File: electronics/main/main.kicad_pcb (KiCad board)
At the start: 2 copper layers, 113 parts, among them IC1 ATMEGA8-P, J1 CABLE, J2 CABLE, J3 CABLE, J4 CABLE, J5 CABLE, J6 CABLE, J7 CABLE, J8 CABLE, P1 5v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

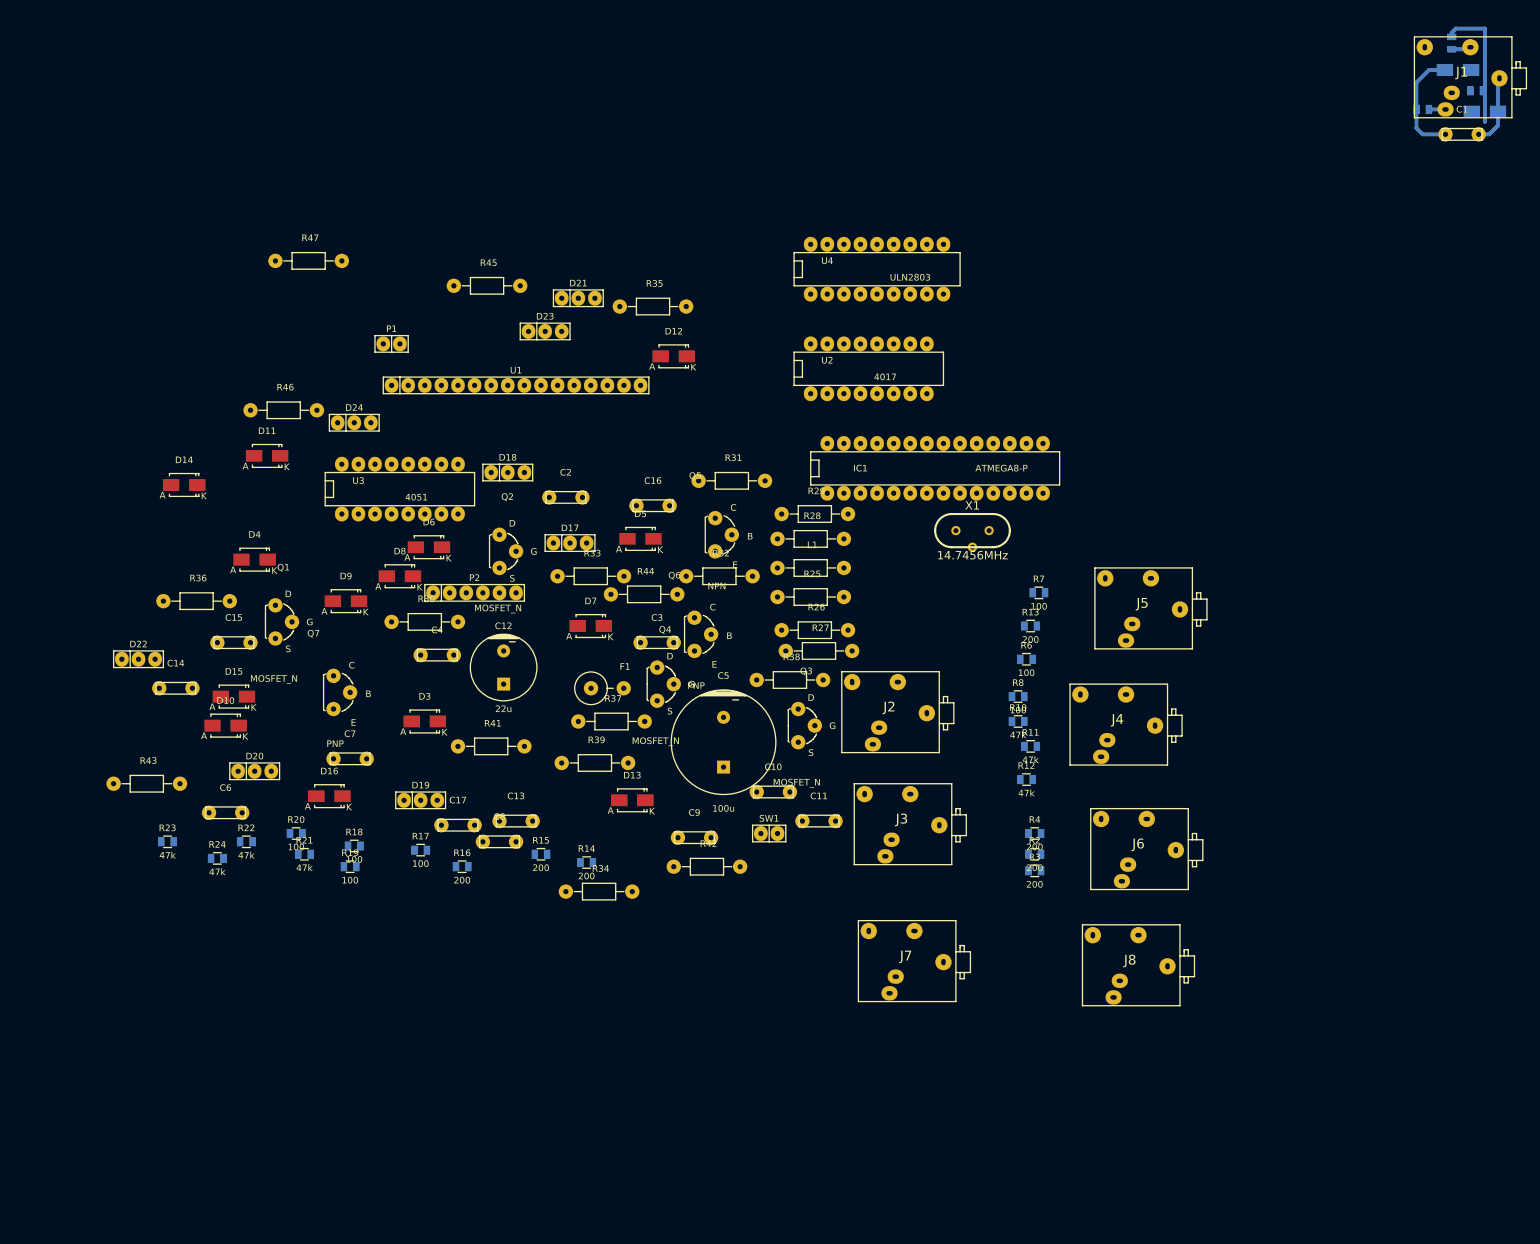
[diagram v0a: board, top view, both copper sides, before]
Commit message: draw inputs on pcb
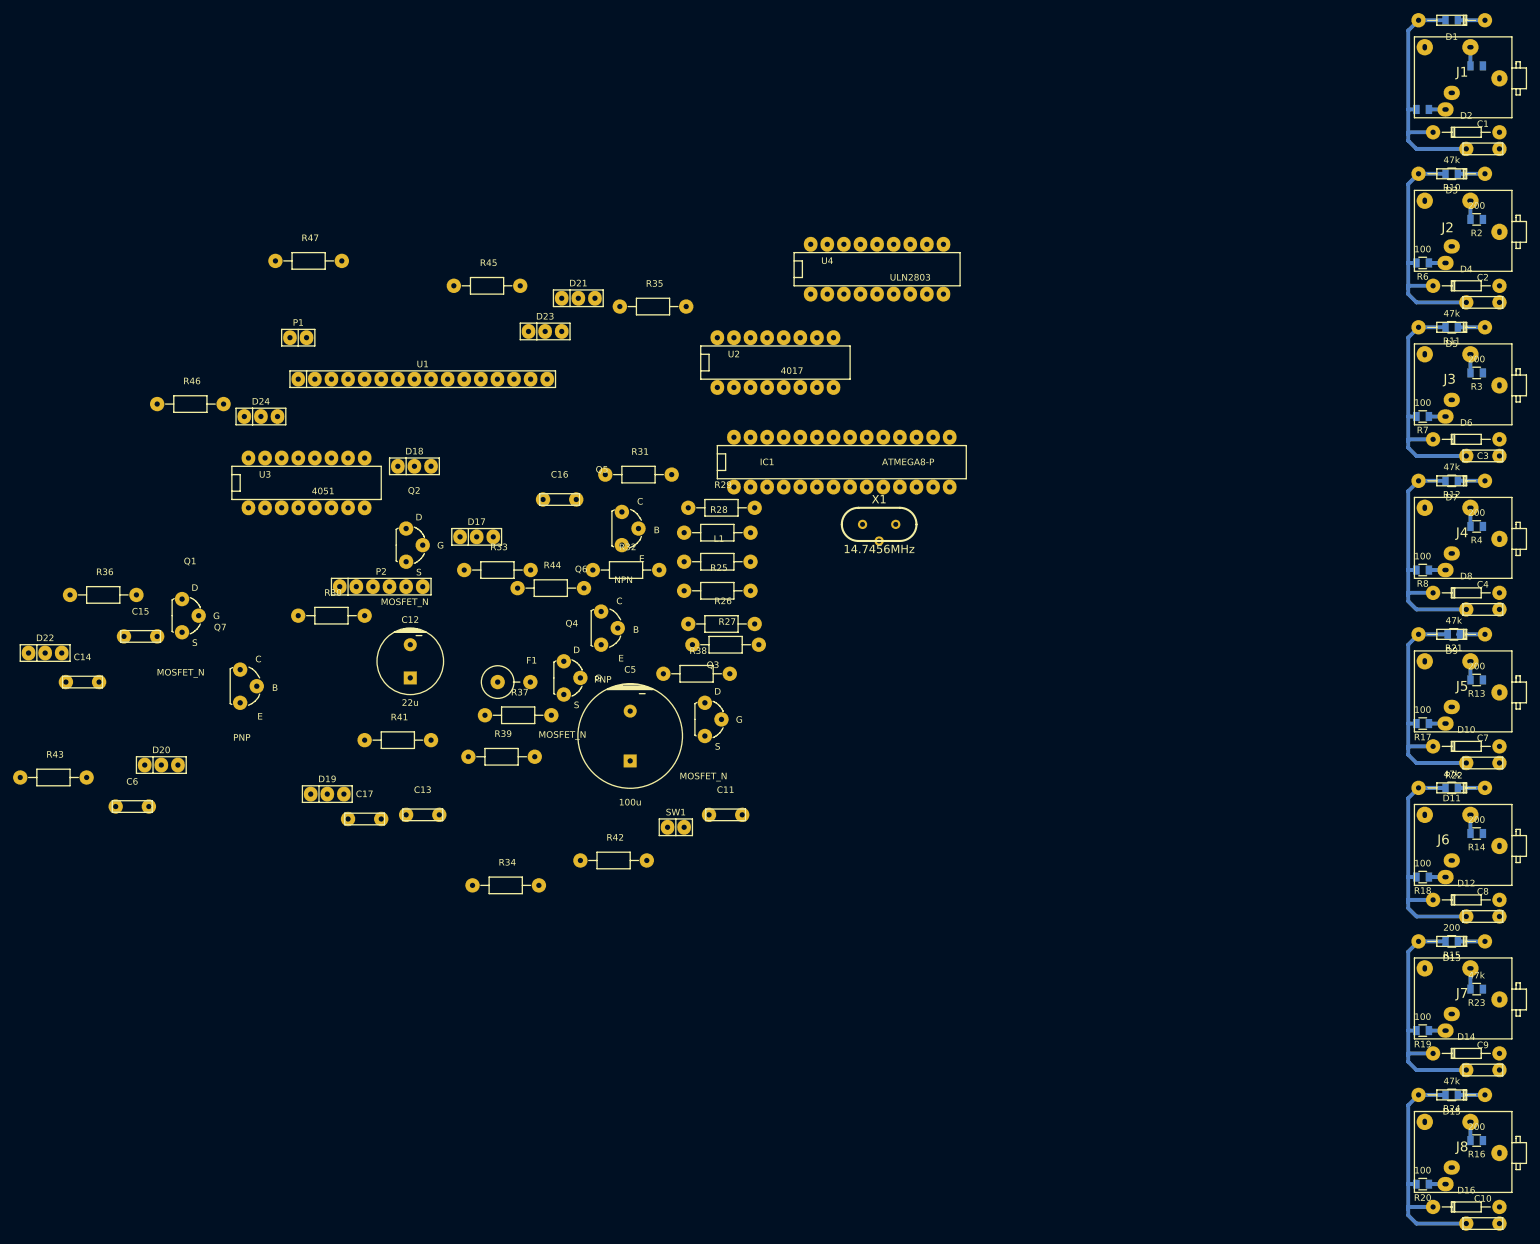
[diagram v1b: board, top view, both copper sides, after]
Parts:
- D1, D2: footprint Diodes_SMD:Diode-SMA_Standard -> Diodes_ThroughHole:Diode_DO-35_SOD27_Horizontal_RM10; moved to F.Cu
- D10, D11, D12, D13, D14, D15, D16, D3, D4, D5, D6, D7, D8, D9: footprint Diodes_SMD:Diode-SMA_Standard -> Diodes_ThroughHole:Diode_DO-35_SOD27_Horizontal_RM10
- moved D14 214.6 mm to (274.3, 175.3), turned to 180 degrees
- moved R23 201.6 mm to (275.9, 165.4), turned to 180 degrees
- moved D15 196.1 mm to (272.1, 181.6)
- moved R24 192.3 mm to (272.1, 181.6), turned to 180 degrees
- moved D4 190.1 mm to (274.3, 57.8), turned to 180 degrees
- moved D10 189.9 mm to (274.3, 128.3), turned to 180 degrees
- moved D11 188.3 mm to (272.1, 134.6)
- moved D16 185.0 mm to (274.3, 198.8), turned to 180 degrees
- moved R22 184.7 mm to (272.1, 134.6), turned to 180 degrees
- moved R20 180.6 mm to (267.7, 195.3), turned to 180 degrees
- moved R21 179.1 mm to (272.4, 111.1), turned to 180 degrees
- moved D3 178.1 mm to (272.1, 40.6)
- moved C7 173.4 mm to (276.9, 130.8)
- moved D9 169.3 mm to (272.1, 111.1)
- moved R19 166.1 mm to (267.7, 171.8), turned to 180 degrees
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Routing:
- net /IN6: track 0.00 -> 38.0 mm
- net /IN7: track 0.00 -> 38.0 mm
- net /IN2: track 0.00 -> 38.0 mm
- net /IN5: track 0.00 -> 38.0 mm
- net /IN4: track 0.00 -> 38.0 mm
- net /IN8: track 0.00 -> 38.0 mm
- net /IN3: track 0.00 -> 38.0 mm
- net /IN1: track 17.0 -> 38.0 mm
- net VCC: track 21.7 -> 33.0 mm
- net GND: track 10.8 -> 0.00 mm
- net Net-(J5-Pad3): track 0.00 -> 2.86 mm
- net Net-(J3-Pad3): track 0.00 -> 2.86 mm
- net Net-(J2-Pad3): track 0.00 -> 2.86 mm
- net Net-(J4-Pad3): track 0.00 -> 2.86 mm
- net Net-(J8-Pad3): track 0.00 -> 2.86 mm
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
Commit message: draw led control
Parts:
- D17, D18, D19, D20, D21, D22, D23, D24: value BI_LED -> BI_LED2
- Q5, Q6, Q7: footprint Housings_TO-92:TO-92-Bipolar-molded-wide-CBE -> Housings_TO-92:TO-92-Free-molded-wide
- moved D1 225.1 mm to (47.1, 24.6), turned to 90 degrees
- moved R9 225.1 mm to (47.1, 24.6), turned to 270 degrees
- moved R1 221.8 mm to (54.1, 20.8), turned to 270 degrees
- moved J1 217.7 mm to (56.0, 23.0), turned to 90 degrees
- moved C1 210.7 mm to (66.8, 19.8), turned to 90 degrees
- moved D2 210.4 mm to (64.3, 22.4), turned to 270 degrees
- moved R5 206.9 mm to (60.8, 29.1), turned to 270 degrees
- moved D3 202.1 mm to (70.6, 24.6), turned to 90 degrees
- moved R10 202.1 mm to (70.6, 24.6), turned to 270 degrees
- moved R2 200.1 mm to (77.6, 20.8), turned to 270 degrees
- moved J2 196.0 mm to (79.5, 23.0), turned to 90 degrees
- moved C2 190.9 mm to (90.3, 19.8), turned to 90 degrees
- moved D4 189.9 mm to (87.8, 22.4), turned to 270 degrees
- moved C10 187.1 mm to (231.3, 19.8), turned to 90 degrees
- moved R6 185.1 mm to (84.3, 29.1), turned to 270 degrees
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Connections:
- D18 pad 1: Net-(D17-Pad1) -> Net-(D18-Pad1)
- D18 pad 2: Net-(D18-Pad2) -> Net-(D17-Pad2)
- D19 pad 1: Net-(D17-Pad1) -> Net-(D19-Pad1)
- D19 pad 2: Net-(D19-Pad2) -> Net-(D17-Pad2)
- D20 pad 1: Net-(D17-Pad1) -> Net-(D20-Pad1)
- D20 pad 2: Net-(D20-Pad2) -> Net-(D17-Pad2)
- D21 pad 1: Net-(D17-Pad1) -> Net-(D21-Pad1)
- D21 pad 2: Net-(D21-Pad2) -> Net-(D17-Pad2)
- D22 pad 1: Net-(D17-Pad1) -> Net-(D22-Pad1)
- D22 pad 2: Net-(D22-Pad2) -> Net-(D17-Pad2)
- D23 pad 1: Net-(D17-Pad1) -> Net-(D23-Pad1)
- D23 pad 2: Net-(D23-Pad2) -> Net-(D17-Pad2)
- D24 pad 1: Net-(D17-Pad1) -> Net-(D24-Pad1)
- D24 pad 2: Net-(D24-Pad2) -> Net-(D17-Pad2)
- R45 pad 2: (no net) -> Net-(Q6-Pad3)
- R47 pad 1: Net-(D17-Pad1) -> Net-(D17-Pad2)
- R47 pad 2: (no net) -> Net-(Q7-Pad3)
- U1 pad 16: (no net) -> Net-(Q5-Pad3)
- U3 pad 1: /IN5 -> /IN4
- U3 pad 12: /IN4 -> /IN8
- U3 pad 13: /IN1 -> /IN7
- U3 pad 14: /IN2 -> /IN6
- U3 pad 15: /IN3 -> /IN5
- U3 pad 2: /IN7 -> /IN3
- U3 pad 4: /IN8 -> /IN2
- U3 pad 5: /IN6 -> /IN1
- U4 pad 1: /L1 -> /L8
- U4 pad 11: Net-(D24-Pad2) -> Net-(D24-Pad1)
- U4 pad 12: Net-(D23-Pad2) -> Net-(D23-Pad1)
- U4 pad 13: Net-(D22-Pad2) -> Net-(D22-Pad1)
- U4 pad 14: Net-(D21-Pad2) -> Net-(D21-Pad1)
- U4 pad 15: Net-(D20-Pad2) -> Net-(D20-Pad1)
- U4 pad 16: Net-(D19-Pad2) -> Net-(D19-Pad1)
- U4 pad 17: Net-(D18-Pad2) -> Net-(D18-Pad1)
- U4 pad 18: Net-(D17-Pad2) -> Net-(D17-Pad1)
- U4 pad 2: /L2 -> /L7
- U4 pad 3: /L3 -> /L6
- U4 pad 4: /L4 -> /L5
- U4 pad 5: /L5 -> /L4
- U4 pad 6: /L6 -> /L3
- U4 pad 7: /L7 -> /L2
- U4 pad 8: /L8 -> /L1
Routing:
- net /IN8: track 38.0 -> 132.0 mm
- net /IN1: track 38.0 -> 117.9 mm
- net /IN7: track 38.0 -> 103.3 mm
- net /IN2: track 38.0 -> 93.7 mm
- net /IN6: track 38.0 -> 82.9 mm
- net GND: track 0.00 -> 33.4 mm
- net /IN3: track 38.0 -> 65.8 mm
- net /IN5: track 38.0 -> 57.9 mm
- net Net-(Q7-Pad2): track 0.00 -> 16.7 mm
- net /L8: track 0.00 -> 15.6 mm
- net /IN4: track 38.0 -> 42.8 mm
- net Net-(D20-Pad1): track 0.00 -> 4.71 mm
- net Net-(D21-Pad1): track 0.00 -> 4.71 mm
- net /L7: track 0.00 -> 4.45 mm
- net /L6: track 0.00 -> 4.45 mm
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
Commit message: draw some more of the pcb
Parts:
- R25, R26, R27, R28, R35, R36: footprint Resistors_ThroughHole:Resistor_Horizontal_RM10mm -> Resistors_SMD:R_0805; moved to B.Cu
- moved R46 125.7 mm to (126.7, 65.1)
- moved Q7 123.5 mm to (125.7, 54.3)
- moved R47 123.2 mm to (121.6, 44.8)
- moved R42 122.9 mm to (123.2, 65.1)
- moved Q1 121.6 mm to (183.2, 47.6), turned to 180 degrees
- moved R44 120.4 mm to (119.4, 65.1)
- moved Q6 119.4 mm to (118.4, 54.3)
- moved D19 118.5 mm to (95.9, 44.1)
- moved D20 118.5 mm to (98.4, 44.1)
- moved D23 118.5 mm to (106.0, 44.1)
- moved D24 118.5 mm to (108.6, 44.1)
- moved D17 118.5 mm to (90.8, 44.1)
- moved D18 118.5 mm to (93.3, 44.1)
- moved D21 118.5 mm to (101.0, 44.1)
- moved D22 118.5 mm to (103.5, 44.1)
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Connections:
- IC1 pad 27: /LED_CLK -> /LED_A2
- IC1 pad 28: /LED_RESET -> /LED_A1
- IC1 pad 4: /LED_A1 -> /LED_RESET
- IC1 pad 5: /LED_A2 -> /LED_CLK
- U1 pad 13: Net-(IC1-Pad15) -> Net-(IC1-Pad16)
- U1 pad 14: Net-(IC1-Pad16) -> Net-(IC1-Pad15)
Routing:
- net VCC: track 33.0 -> 109.5 mm
- net GND: track 33.4 -> 99.3 mm
- net /LED_CLK: track 0.00 -> 56.3 mm
- net +3.3VP: track 0.00 -> 49.4 mm
- net /LED_RESET: track 0.00 -> 49.1 mm
- net /LED_A2: track 0.00 -> 34.9 mm
- net Net-(IC1-Pad13): track 0.00 -> 33.7 mm
- net Net-(IC1-Pad16): track 0.00 -> 33.1 mm
- net /MOSI: track 0.00 -> 32.9 mm
- net Net-(D17-Pad2): track 0.00 -> 32.6 mm
- net Net-(IC1-Pad14): track 0.00 -> 31.4 mm
- net Net-(IC1-Pad11): track 0.00 -> 30.9 mm
- net Net-(IC1-Pad15): track 0.00 -> 30.1 mm
- net /SCK: track 0.00 -> 29.1 mm
- net Net-(IC1-Pad12): track 0.00 -> 28.6 mm
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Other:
- net class Default: clearance 0.2 -> 0.05
- rule trace_clearance: 0.2 -> 0.05

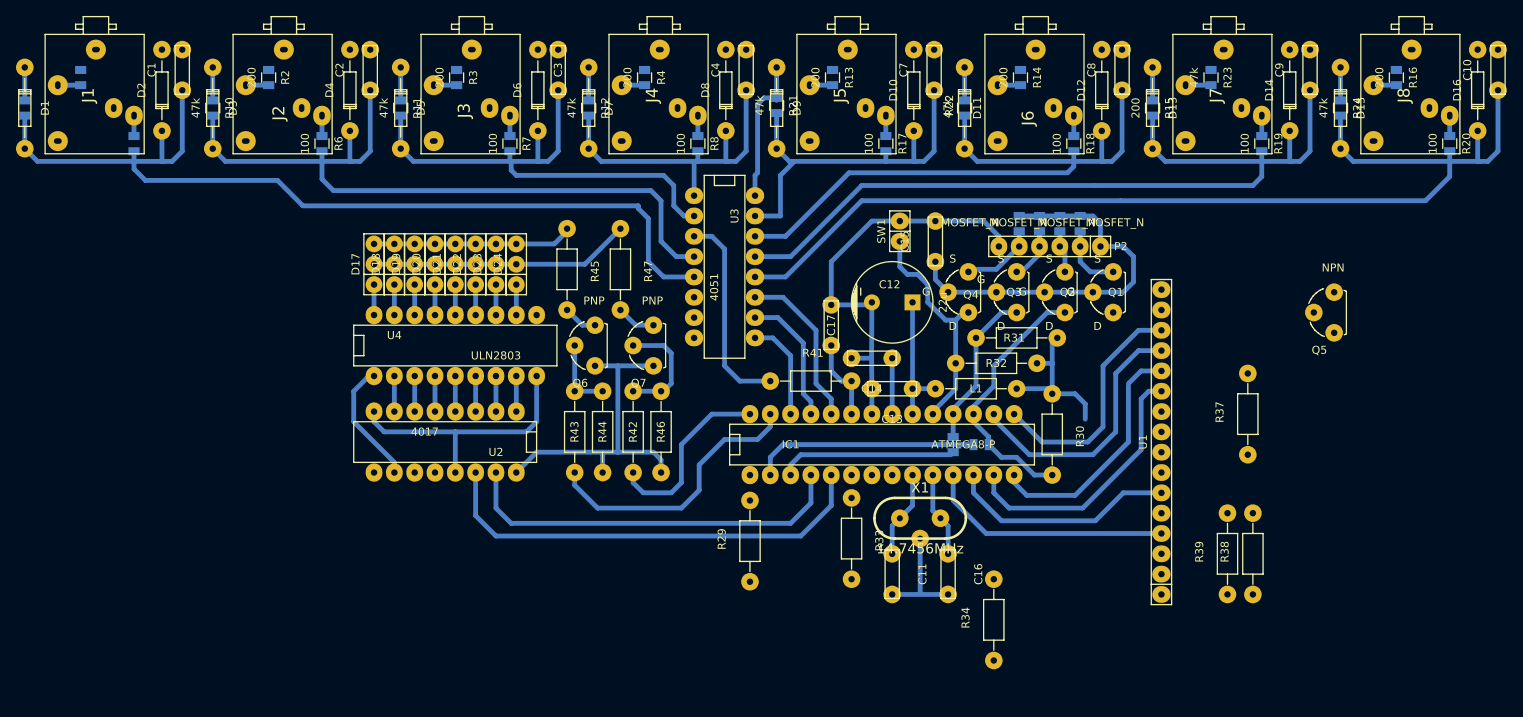
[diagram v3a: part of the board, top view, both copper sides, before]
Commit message: add some ground
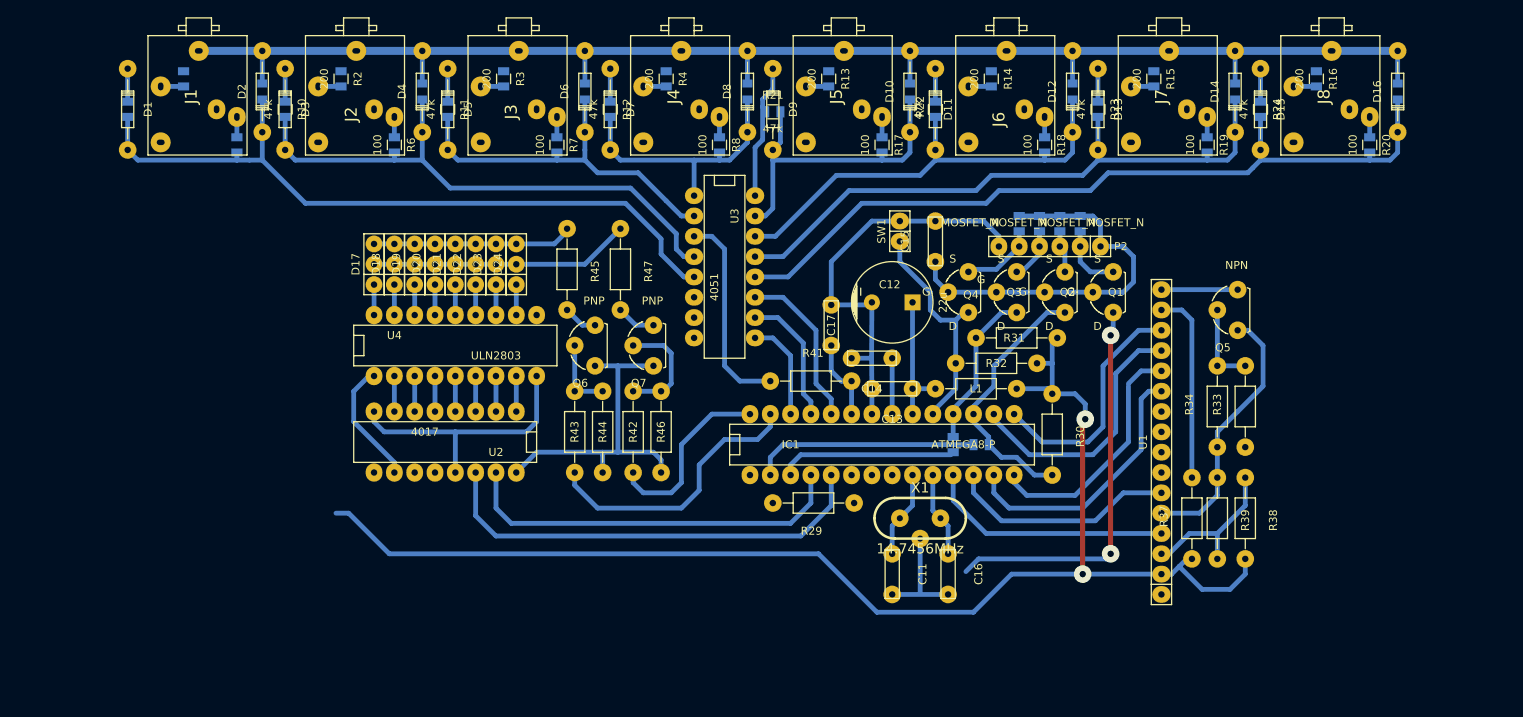
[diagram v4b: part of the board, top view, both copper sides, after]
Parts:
- C1, C10, C2, C3, C4, C7, C8, C9: footprint Capacitors_ThroughHole:Capacitor6MMDiscRM5 -> Capacitors_SMD:C_0805; moved to B.Cu
- moved R33 51.9 mm to (199.7, 61.9), turned to 90 degrees
- moved R34 38.6 mm to (196.2, 61.9)
- moved R37 14.8 mm to (193.0, 75.9)
- moved R23 14.7 mm to (181.3, 24.8)
- moved R1 12.9 mm to (67.0, 21.0)
- moved D1 12.9 mm to (60.0, 24.8)
- moved R9 12.9 mm to (60.0, 24.8)
- moved J1 12.9 mm to (68.9, 23.2)
- moved R5 12.9 mm to (73.7, 29.2)
- moved C10 12.8 mm to (218.8, 22.5)
- moved D2 12.5 mm to (76.8, 22.5)
- moved Q5 12.1 mm to (198.8, 49.8)
- moved C1 10.4 mm to (76.8, 22.5)
- moved R20 10.0 mm to (215.3, 29.2)
- moved D15 10.0 mm to (201.6, 24.8)
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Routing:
- net GND: track 99.3 -> 315.2 mm
- net VCC: track 109.5 -> 255.9 mm, vias 0 -> 2
- net /RESET: track 0.00 -> 49.3 mm, vias 0 -> 2
- net /IN8: track 132.0 -> 99.7 mm
- net /IN1: track 117.9 -> 91.2 mm
- net /IN6: track 82.1 -> 57.0 mm
- net /IN7: track 103.3 -> 78.4 mm
- net Net-(R37-Pad2): track 0.00 -> 24.0 mm
- net /IN2: track 93.7 -> 71.4 mm
- net Net-(R38-Pad1): track 0.00 -> 19.6 mm
- net /IN3: track 65.8 -> 46.9 mm
- net Net-(Q5-Pad2): track 0.00 -> 10.5 mm
- net Net-(Q5-Pad3): track 0.00 -> 9.53 mm
- net /IN4: track 42.8 -> 33.5 mm
- net /IN5: track 48.7 -> 40.2 mm
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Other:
- net class Power added: clearance 0.05, trace_width 1, via_dia 2.2, via_drill 0.8

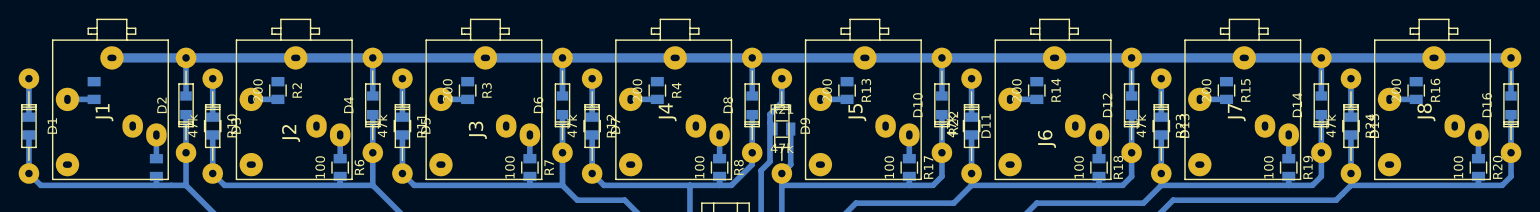
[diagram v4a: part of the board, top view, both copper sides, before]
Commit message: now remain vcc and gnd
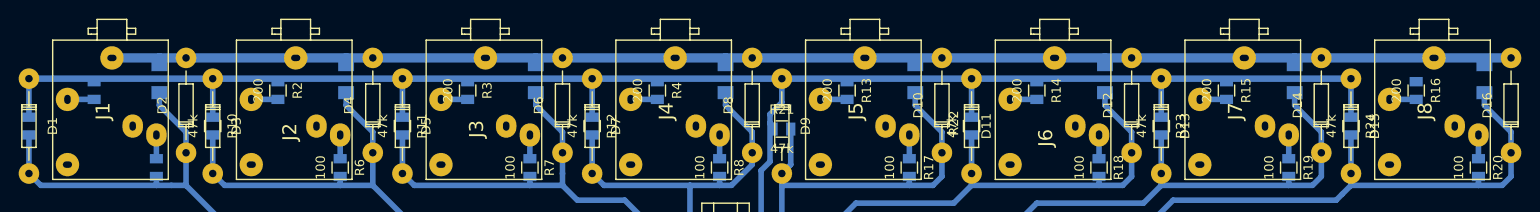
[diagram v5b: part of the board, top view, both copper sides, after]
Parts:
- C1, C10, C2, C3, C4, C7, C8, C9: footprint Capacitors_SMD:C_0805 -> Capacitors_SMD:C_1206
- moved C7 4.04 mm to (154.9, 19.7)
- moved C8 4.04 mm to (175.3, 19.7)
- moved C2 4.04 mm to (94.0, 19.7)
- moved C3 4.04 mm to (114.3, 19.7)
- moved C1 4.04 mm to (74.0, 19.7)
- moved C10 4.04 mm to (215.9, 19.7)
- moved C4 4.04 mm to (134.6, 19.7)
- moved C9 4.04 mm to (195.6, 19.7)
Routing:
- net VCC: track 255.9 -> 397.5 mm
- net GND: track 315.2 -> 287.5 mm
- net /IN6: track 57.0 -> 60.5 mm
- net /IN5: track 40.2 -> 43.7 mm
- net /IN2: track 71.4 -> 74.9 mm
- net /IN8: track 99.7 -> 103.3 mm
- net /IN7: track 78.4 -> 81.9 mm
- net /IN4: track 33.5 -> 37.0 mm
- net /IN3: track 46.9 -> 50.4 mm
- net /IN1: track 91.2 -> 94.7 mm
